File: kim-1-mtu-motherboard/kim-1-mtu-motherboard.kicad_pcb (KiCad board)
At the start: 2 copper layers, 210 x 273 mm, 117 parts, among them J1 Power_Connector, J10 GND, J11 K7, J12 DECEN, J13 K7, J14 DECEN, J2 Audio Out, J3 Audio In, J4 Audio HI/LO, J5 Audio Loop, J6 Decode, J7 Daughterboard, J8 RESET, J9 GND, P1 EXP_BOARD, P10 EXP_BOARD, P11 EXP_BOARD, P12 KIM-1, P13 KIM_EXP, P14 KIM_APPL, P2 EXP_BOARD, P3 EXP_BOARD, P4 EXP_BOARD, P5 EXP_BOARD, P6 KIM-1, P7 EXP_BOARD, P8 EXP_BOARD, P9 EXP_BOARD, U1 74HCT541, U2 74HCT541, U3 74HCT541, U4 74LS245, U5 74LS07

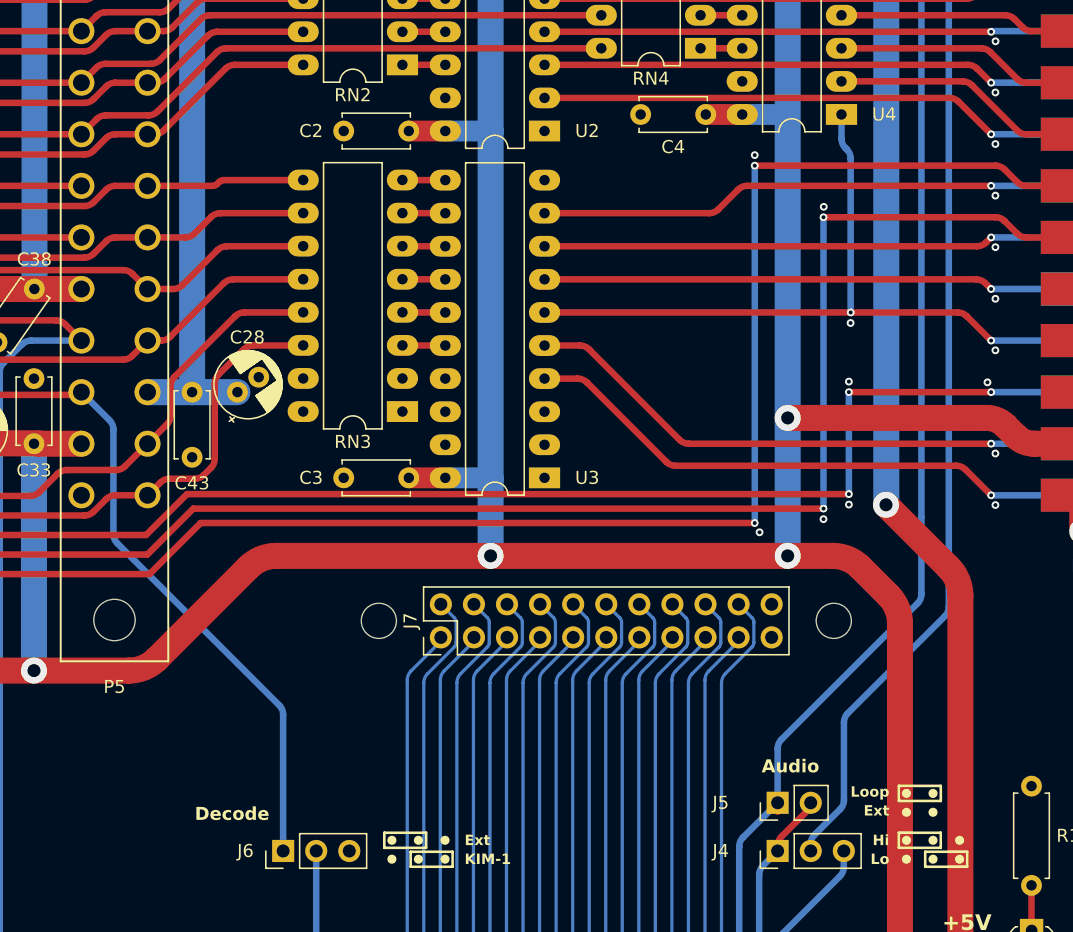
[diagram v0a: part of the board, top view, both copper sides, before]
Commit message: Disable data bus transceiver when DECEN or K7 active (low). Should fix issue #2
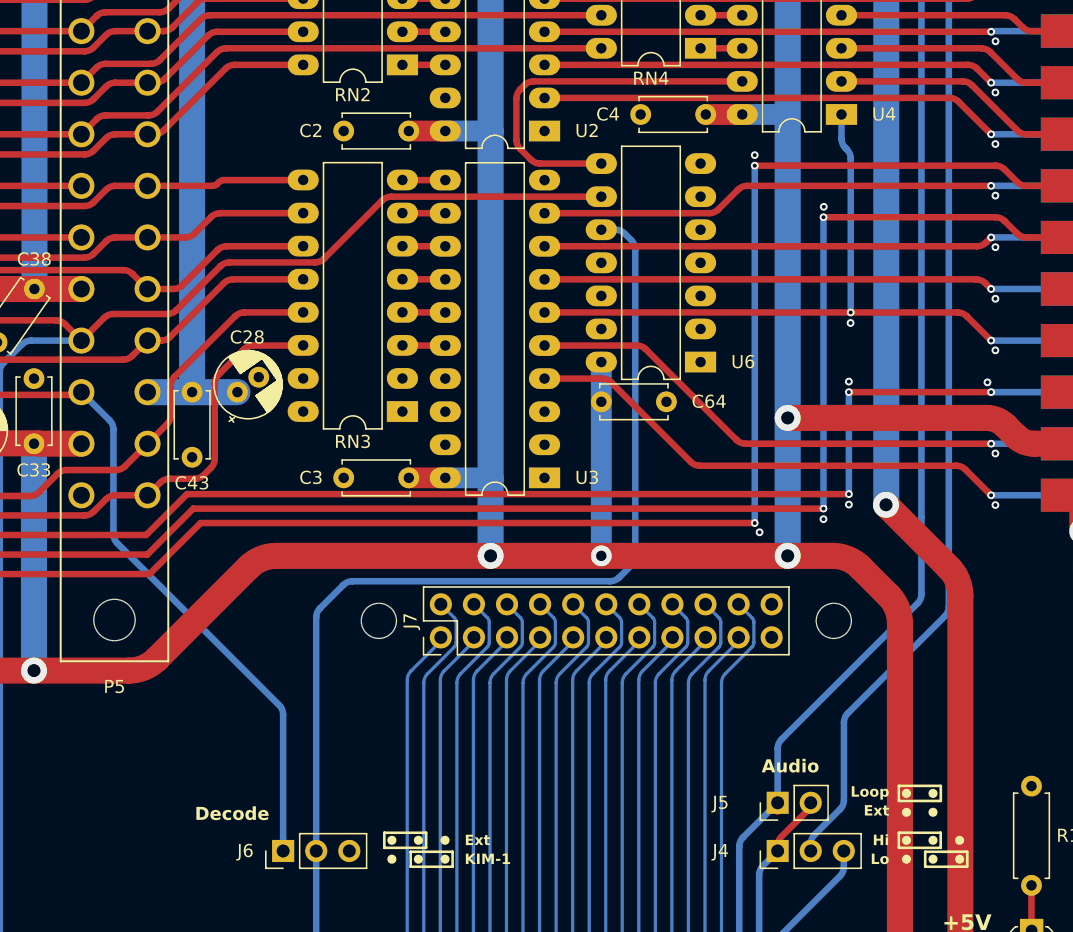
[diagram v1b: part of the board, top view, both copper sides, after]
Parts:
- added C64: 100nF, Capacitor_THT:C_Disc_D5.0mm_W2.5mm_P5.00mm, F.Cu at (212.6, 147.9)
- added U6: 74LS00, Package_DIP:DIP-14_W7.62mm_LongPads, F.Cu at (220.2, 144.8)
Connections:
- U4 pad 19: GND -> Net-(U4-CE)
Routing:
- net /DECEN: track 287.2 -> 358.8 mm
- net /K7: track 346.7 -> 390.9 mm
- net Net-(U4-CE): track 0.00 -> 28.6 mm
- net +5V: track 933.3 -> 948.2 mm, vias 16 -> 17
